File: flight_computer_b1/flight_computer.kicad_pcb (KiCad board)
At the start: 4 copper layers, 90.3 x 56 mm, 63 parts, among them J1 Pi Connector, J2 Conn_01x03, J3 Conn_02x02_Odd_Even, J4 DB25_Socket, J5 DB25_Socket, U1 IRLML6344TRPBF, U2 IRLML6344TRPBF, U3 IRLML6344TRPBF, U4 IRLML6344TRPBF, U5 LMR51430XDDCR, U6 MIC94161YCS-TR

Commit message: flight computer changes
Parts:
- J4: footprint Connector_Dsub:DSUB-25_Socket_Horizontal_P2.77x2.84mm_EdgePinOffset4.94mm_Housed_MountingHolesOffset4.94mm -> Connector_Dsub:DSUB-25_Socket_Vertical_P2.77x2.84mm_MountingHoles
- moved R16 72.1 mm to (190.9, 77.2)
- moved R17 72.1 mm to (190.9, 79.7)
- moved R18 72.1 mm to (190.9, 82.2)
- moved R19 72.1 mm to (190.9, 84.7)
- moved R24 72.1 mm to (202.9, 77.2)
- moved R25 72.1 mm to (202.9, 79.7)
- moved R26 72.1 mm to (202.9, 82.2)
- moved R27 72.1 mm to (202.9, 84.7)
- moved U6 72.1 mm to (208.2, 77.5)
- moved R36 72.1 mm to (196.9, 77.2)
- moved R37 72.1 mm to (196.9, 79.7)
- moved R38 72.1 mm to (196.9, 82.2)
- moved R39 72.1 mm to (196.9, 84.7)
- moved R5 54.4 mm to (167.5, 93.1), turned to -90 degrees
- moved R6 51.6 mm to (165.0, 92.1), turned to 180 degrees
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
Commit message: flight computer updates
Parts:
- added C10: 4.7pf, Capacitor_SMD:C_0603_1608Metric, F.Cu at (194.4, 81.5)
- added C11: 4.7pf, Capacitor_SMD:C_0603_1608Metric, F.Cu at (194.4, 84.0)
- added C5: 0.1uF, Capacitor_SMD:C_0603_1608Metric, F.Cu at (194.4, 86.5)
- added C6: 10uF, Capacitor_SMD:C_0603_1608Metric, F.Cu at (194.4, 89.0)
- added C7: 10uF, Capacitor_SMD:C_0603_1608Metric, F.Cu at (194.4, 91.5)
- added C8: 0.1uF, Capacitor_SMD:C_0603_1608Metric, F.Cu at (194.4, 94.0)
- added C9: 22nf, Capacitor_SMD:C_0603_1608Metric, F.Cu at (194.4, 79.0)
- added CR5: ST490ABDR, avi_lib:SO-8_STM, F.Cu at (126.2, 122.8)
- added D1: LED, Capacitor_SMD:C_0603_1608Metric, F.Cu at (194.4, 96.5)
- added R40: 100, Resistor_SMD:R_0603_1608Metric, F.Cu at (194.4, 99.0)
- added U6: ADS1158IRTCR, avi_lib:RTC0048A-IPC_A, F.Cu at (139.0, 85.8)
- added Y1: 32.768kHz, avi_lib:XTAL_MC-306_32.7680K-A0_ROHS, F.Cu at (148.7, 85.0)
- moved R28 70.5 mm to (137.0, 93.5), turned to 90 degrees
- moved R36 70.2 mm to (128.0, 90.8)
- moved R37 69.6 mm to (128.0, 89.3), turned to 180 degrees
- moved R38 69.0 mm to (128.0, 86.3)
- moved R39 69.0 mm to (128.0, 87.8), turned to 180 degrees
- moved R29 68.9 mm to (138.5, 93.5), turned to -90 degrees
- moved R31 67.5 mm to (140.0, 93.5), turned to -90 degrees
- moved R30 65.9 mm to (141.5, 93.5), turned to 90 degrees
- moved R34 64.6 mm to (130.7, 93.5), turned to 90 degrees
- moved R35 63.2 mm to (132.2, 93.5), turned to -90 degrees
- moved R33 61.6 mm to (133.7, 93.5), turned to -90 degrees
- moved R32 60.2 mm to (135.2, 93.5), turned to 90 degrees
- moved R22 58.1 mm to (143.2, 93.5), turned to 90 degrees
- moved R23 56.8 mm to (144.7, 93.5), turned to -90 degrees
- moved R15 56.4 mm to (157.1, 92.8)
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- renumbered J3 to J2, J2 to J3, U6 to U7

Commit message: flight computer changes
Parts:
- added U8: MCP6001-OT, Package_TO_SOT_SMD:SOT-23-5, F.Cu at (121.1, 82.1)
- added U9: MCP6001-OT, Package_TO_SOT_SMD:SOT-23-5, F.Cu at (125.8, 82.1)
- J4, J5: moved to B.Cu
- moved J5 41.6 mm to (144.1, 135.4), turned to 0 degrees
- moved J4 12.4 mm to (106.0, 115.9)
- moved R12 1.62 mm to (158.6, 90.4)
- moved R13 1.62 mm to (158.6, 91.9)
- moved R14 1.62 mm to (158.6, 94.9)
- moved R15 1.62 mm to (158.6, 93.4)
- moved R16 1.62 mm to (158.6, 88.6)
- moved R17 1.62 mm to (158.6, 87.1)
- moved R18 1.62 mm to (158.6, 84.1)
- moved R19 1.62 mm to (158.6, 85.6)
- moved R20 1.62 mm to (149.2, 94.1)
- moved R21 1.62 mm to (147.7, 94.1)
- moved R22 1.62 mm to (144.7, 94.1)
- moved R23 1.62 mm to (146.2, 94.1)
- moved R24 1.62 mm to (151.0, 94.1)
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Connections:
- CR5 pad 1: /5V_ISO -> +5V_ISO
- CR5 pad 2: /rs485/UART_RX -> /RS485_UART_RX
- CR5 pad 3: /rs485/UART_TX -> /RS485_UART_TX
- J1 pad 10: unconnected-(J1-Pin_10-Pad10) -> /RS485_UART_RX
- J1 pad 8: unconnected-(J1-Pin_8-Pad8) -> /RS485_UART_TX
- U6 pad 41: unconnected-(U6-ADCINN-Pad41) -> /adc0/ADCINN
- U6 pad 42: unconnected-(U6-ADCINP-Pad42) -> /adc0/ADCINP
- U6 pad 43: unconnected-(U6-MUXOUTN-Pad43) -> /adc0/MUXOUTN
- U6 pad 44: unconnected-(U6-MUXOUTP-Pad44) -> /adc0/MUXOUTP
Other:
- board size 90.3 x 56 mm -> 66 x 56 mm

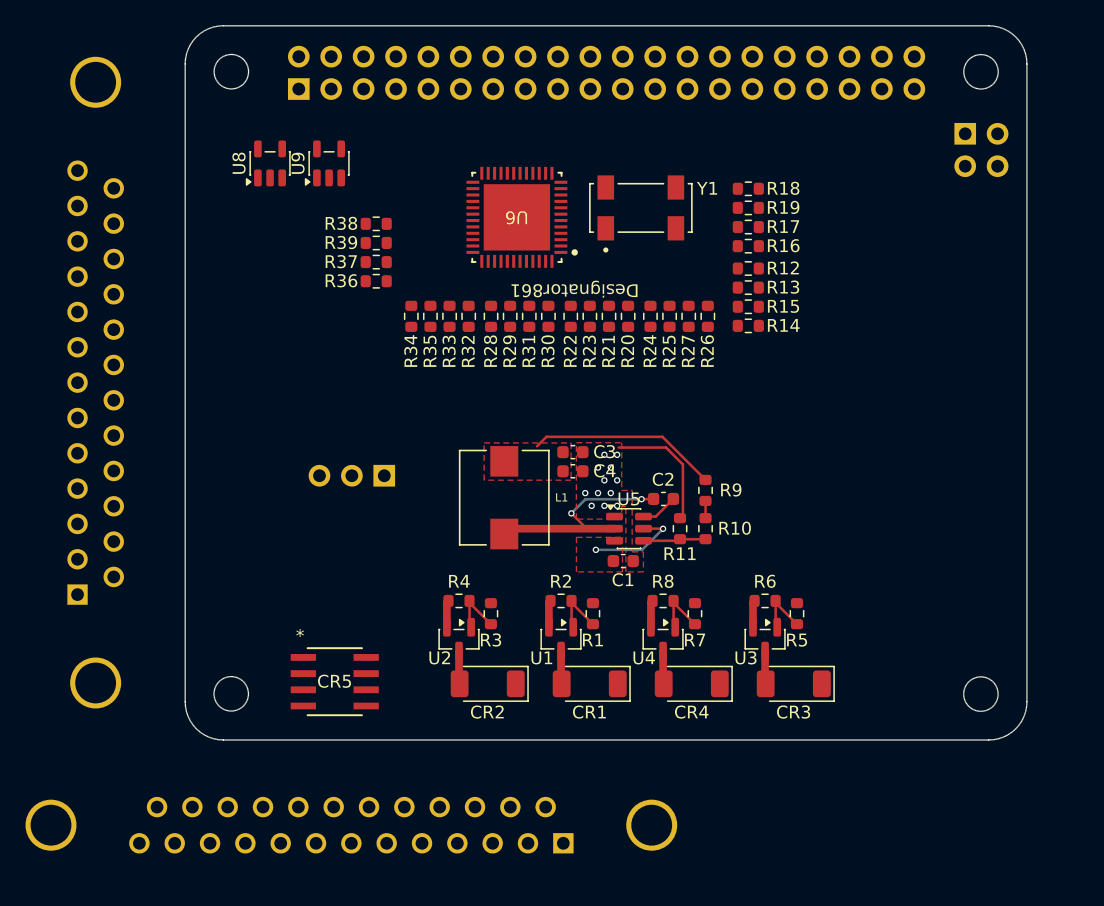
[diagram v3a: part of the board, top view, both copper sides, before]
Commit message: flight computer dimension changes
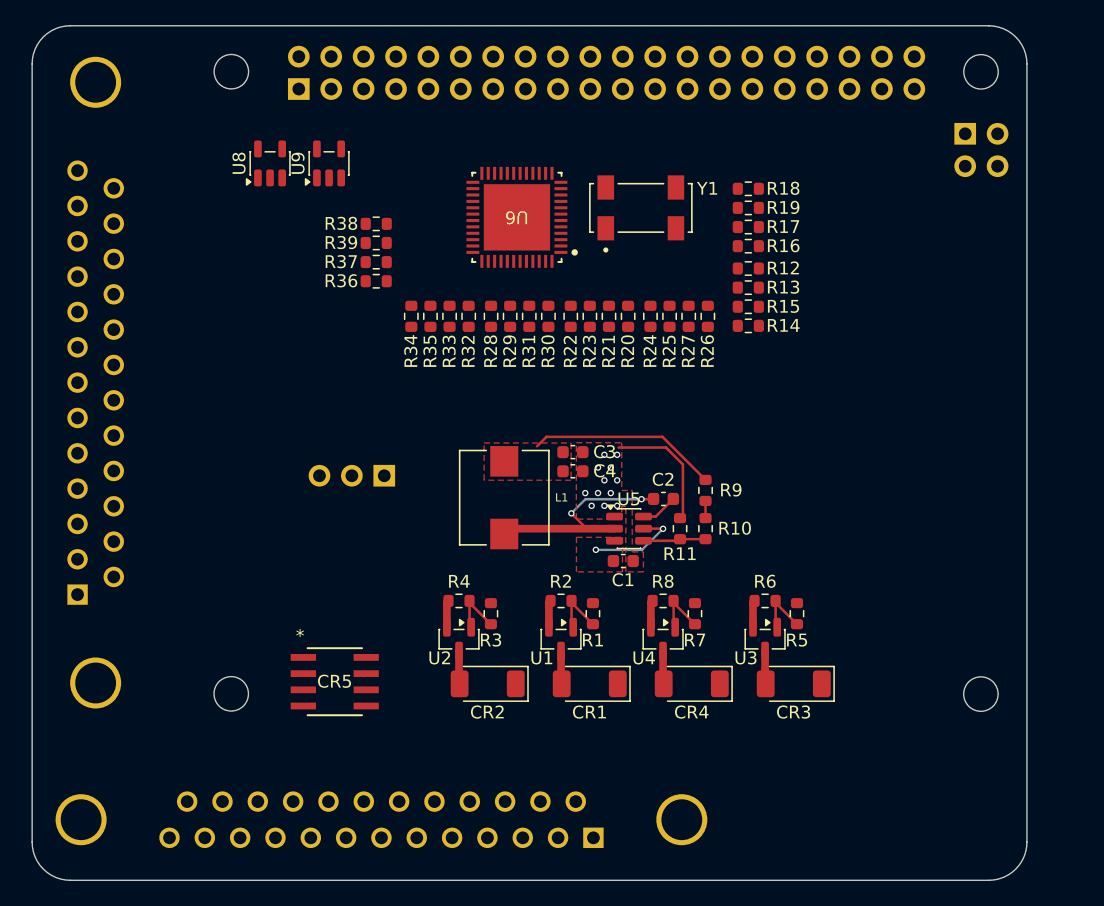
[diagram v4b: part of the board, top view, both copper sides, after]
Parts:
- moved J5 2.40 mm to (146.5, 135.0)
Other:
- board size 66 x 56 mm -> 78 x 67 mm
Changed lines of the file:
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@@
 		(fp_text user "*"
 			(at -2.7178 -3.5814 0)
+			(unlocked yes)
 			(layer "F.SilkS")
 			(effects
@@
 		(fp_text user "*"
 			(at -2.7178 -3.5814 0)
-			(unlocked yes)
 			(layer "F.SilkS")
 			(effects
@@
 			(layer "F.Fab")
 		)
-		(fp_text user "Designator861"
-			(at -4.5212 -5.715 180)
-			(unlocked yes)
-			(layer "F.SilkS")
-			(effects
-				(font
-					(size 1 1)
-					(thickness 0.15)
-				)
-			)
-		)
 		(fp_text user "${REFERENCE}"
 			(at 0 0 180)
@@
 	(footprint "Connector_Dsub:DSUB-25_Socket_Vertical_P2.77x2.84mm_MountingHoles"
 		(layer "B.Cu")
-		(at 144.14 135.43)
+		(at 146.5 135)
 		(descr "25-pin D-Sub connector, straight/vertical, THT-mount, socket (female), pitch 2.77x2.84mm, distance of mounting holes 47.1mm, see https://disti-assets.s3.amazonaws.com/tonar/files/datasheets/16730.pdf")
 		(tags "25-pin D-Sub connector straight vertical THT socket pitch 2.77x2.84mm mounting holes distance 47.1mm")
@@
 	)
 	(gr_arc
-		(start 180.49 124.337176)
-		(mid 179.613422 126.453422)
-		(end 177.497176 127.33)
+		(start 180.49 135.337176)
+		(mid 179.613429 137.453429)
+		(end 177.497176 138.33)
 		(stroke
 			(width 0.0381)
@@
 	)
 	(gr_line
-		(start 177.497176 127.33)
-		(end 117.482824 127.33)
+		(start 180.49 74.322824)
+		(end 180.49 135.337176)
 		(stroke
 			(width 0.0381)
@@
 		(layer "Edge.Cuts")
 	)
-	(gr_line
-		(start 117.482824 71.33)
-		(end 177.497176 71.33)
+	(gr_arc
+		(start 177.497176 71.33)
+		(mid 179.613422 72.206578)
+		(end 180.49 74.322824)
 		(stroke
 			(width 0.0381)
@@
 		(layer "Edge.Cuts")
 	)
-	(gr_line
-		(start 180.49 124.337176)
-		(end 180.49 74.322824)
+	(gr_arc
+		(start 102.49 74.32)
+		(mid 103.366578 72.203754)
+		(end 105.482824 71.327176)
 		(stroke
 			(width 0.0381)
@@
 		(layer "Edge.Cuts")
 	)
-	(gr_arc
-		(start 177.497176 71.33)
-		(mid 179.613422 72.206578)
-		(end 180.49 74.322824)
+	(gr_line
+		(start 102.490001 135.337176)
+		(end 102.49 74.32)
 		(stroke
 			(width 0.0381)
@@
 		(layer "Edge.Cuts")
 	)
-	(gr_arc
-		(start 114.49 74.32)
-		(mid 115.366578 72.203754)
-		(end 117.482824 71.327176)
+	(gr_line
+		(start 177.4972 138.33)
+		(end 105.482824 138.33)
 		(stroke
 			(width 0.0381)
@@
 	)
 	(gr_line
-		(start 114.49 124.334352)
-		(end 114.49 74.32)
+		(start 105.482824 71.327176)
+		(end 177.4972 71.33)
 		(stroke
 			(width 0.0381)
@@
 	)
 	(gr_arc
-		(start 117.482824 127.33)
-		(mid 115.366578 126.453422)
-		(end 114.49 124.337176)
+		(start 105.482824 138.33)
+		(mid 103.366578 137.453422)
+		(end 102.49 135.337176)
 		(stroke
 			(width 0.0381)

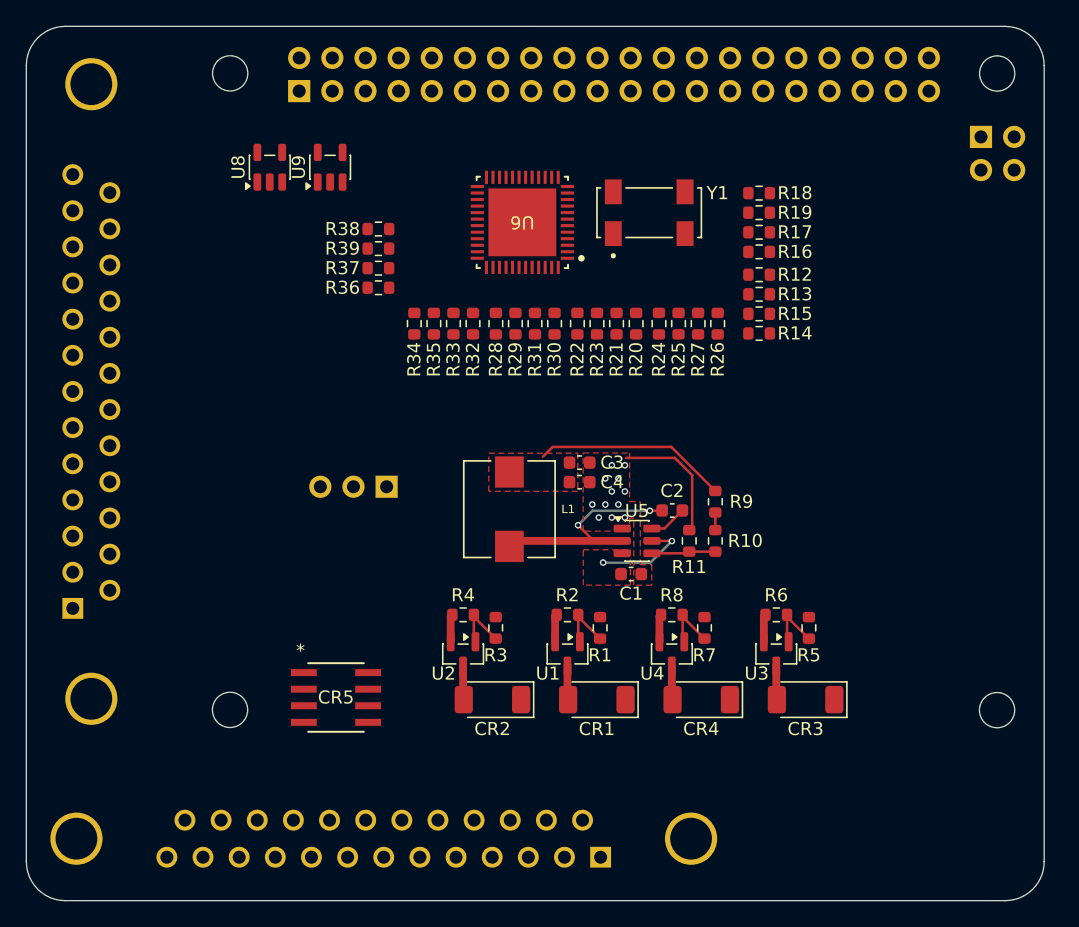
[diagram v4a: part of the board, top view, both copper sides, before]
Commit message: flight computer layout changes
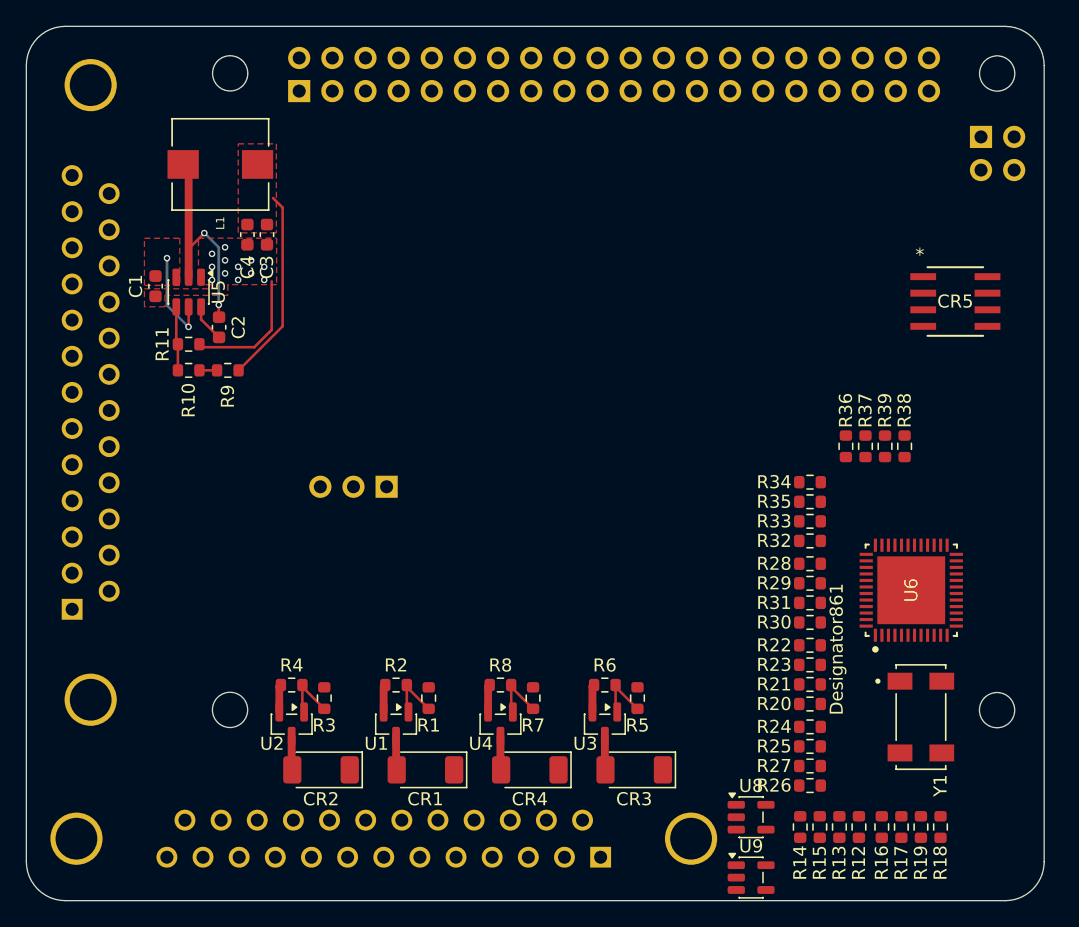
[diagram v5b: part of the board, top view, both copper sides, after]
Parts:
- removed REF** (x4): MountingHole_2.7mm, Mounting_Holes:MountingHole_2.7mm
- added H1: MountingHole, MountingHole:MountingHole_2.7mm_M2.5, F.Cu at (176.9, 74.9)
- added H2: MountingHole, MountingHole:MountingHole_2.7mm_M2.5, F.Cu at (118.1, 74.9)
- added H3: MountingHole, MountingHole:MountingHole_2.7mm_M2.5, F.Cu at (118.1, 123.7)
- added H4: MountingHole, MountingHole:MountingHole_2.7mm_M2.5, F.Cu at (176.9, 123.7)
- moved U9 63.3 mm to (158.0, 136.6), turned to 0 degrees
- moved U8 62.0 mm to (158.0, 131.9), turned to 0 degrees
- moved CR5 56.3 mm to (173.7, 92.4)
- moved R18 50.5 mm to (172.5, 132.7), turned to 90 degrees
- moved R19 48.7 mm to (171.0, 132.7), turned to -90 degrees
- moved R17 46.9 mm to (169.5, 132.7), turned to -90 degrees
- moved R16 45.1 mm to (168.0, 132.7), turned to 90 degrees
- moved Y1 43.9 mm to (171.0, 124.3), turned to 0 degrees
- moved R38 43.6 mm to (169.8, 103.5), turned to -90 degrees
- moved R12 43.0 mm to (166.3, 132.7), turned to 90 degrees
- moved C1 42.6 mm to (112.4, 91.2), turned to -90 degrees
- moved R10 42.4 mm to (114.9, 97.7), turned to 180 degrees
- moved R39 41.7 mm to (168.3, 103.5), turned to 90 degrees
- moved R13 41.3 mm to (164.8, 132.7), turned to -90 degrees
- moved R11 41.2 mm to (114.9, 95.7), turned to 0 degrees
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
